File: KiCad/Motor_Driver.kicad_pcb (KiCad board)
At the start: 2 copper layers, 25 parts, among them J1 Battery Terminal, Q1 NMOS, Q2 NMOS, Q3 NMOS, Q4 NMOS, Q5 NMOS, Q6 NMOS, U1 PS2801-4

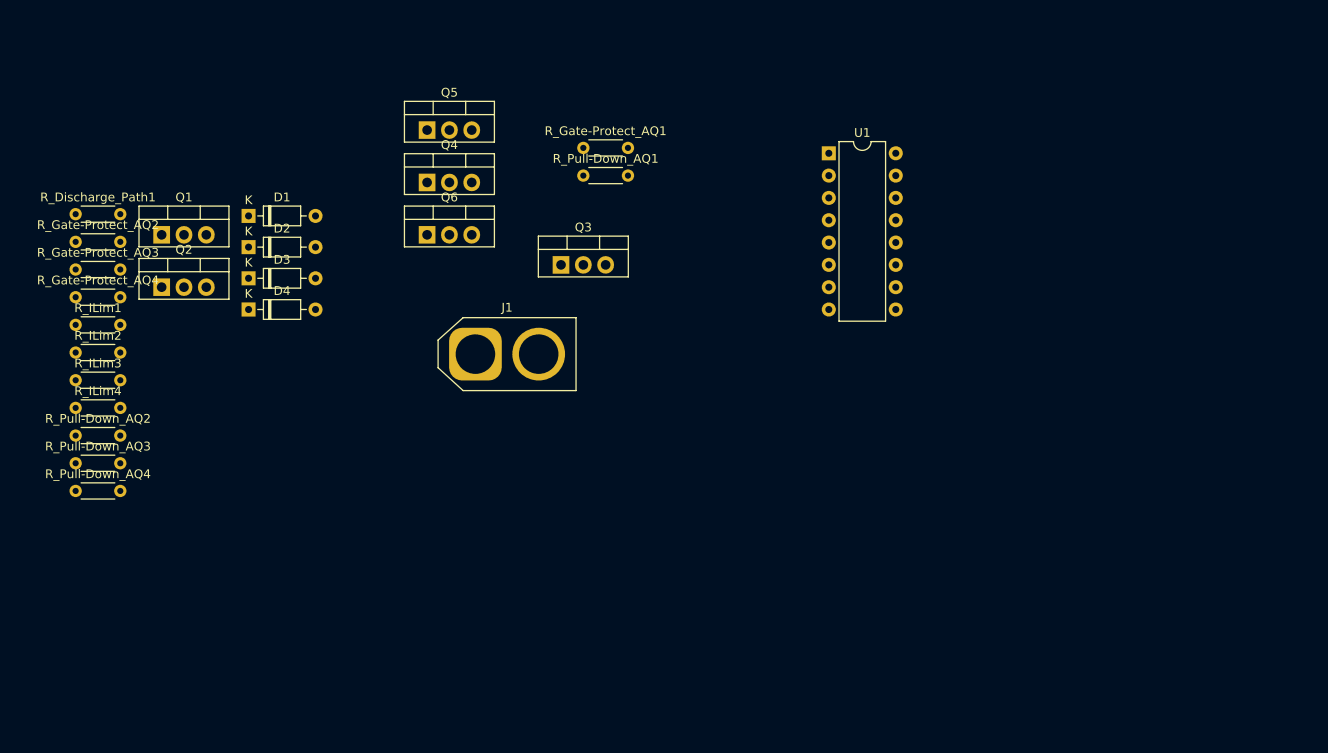
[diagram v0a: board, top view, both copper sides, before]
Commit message: Low Side Driver
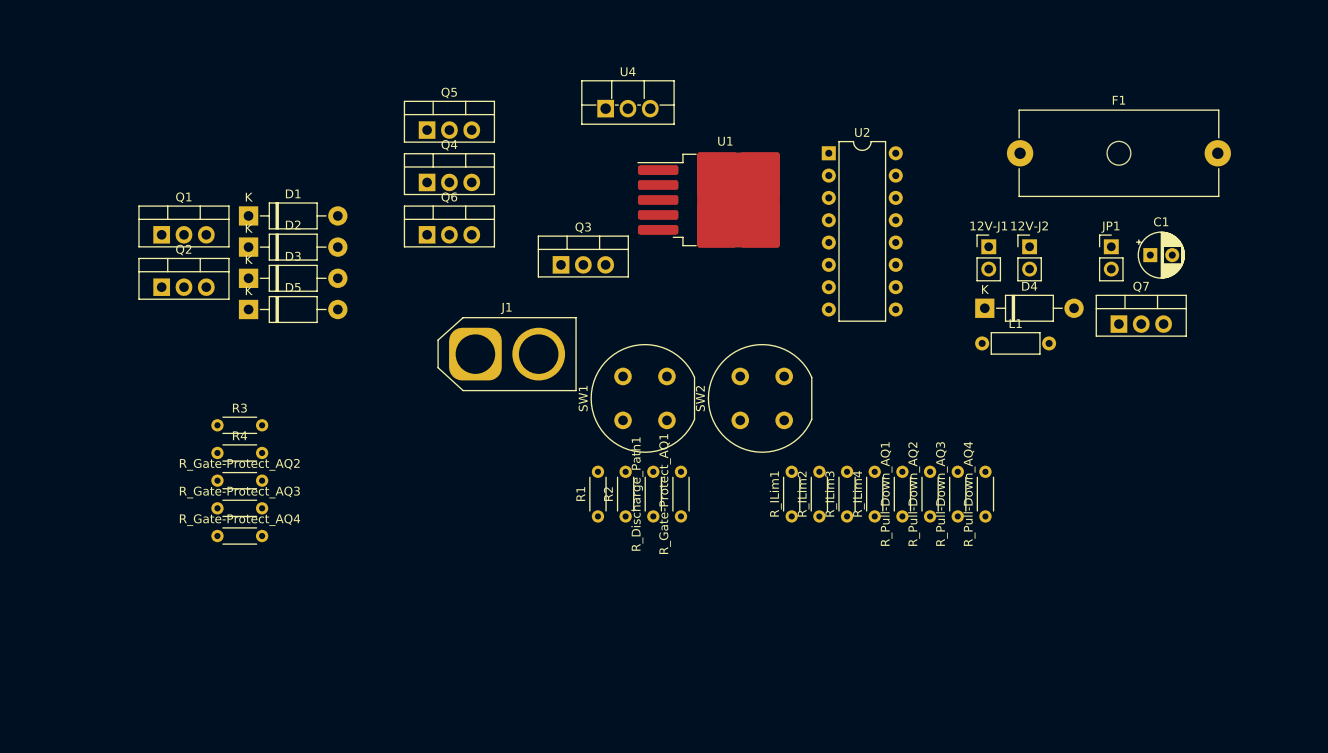
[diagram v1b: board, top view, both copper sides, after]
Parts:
- added 12V-J1: J-12V, Connector_PinHeader_2.54mm:PinHeader_1x02_P2.54mm_Vertical, F.Cu at (142.7, 51.3)
- added 12V-J2: J-12V, Connector_PinHeader_2.54mm:PinHeader_1x02_P2.54mm_Vertical, F.Cu at (147.3, 51.3)
- added C1: 10uF, Capacitor_THT:CP_Radial_D5.0mm_P2.50mm, F.Cu at (161.0, 52.2)
- added D4: 1N4007, Diode_THT:D_DO-41_SOD81_P10.16mm_Horizontal, F.Cu at (142.2, 58.3)
- added F1: Fuse_30A(Slow), Fuse:Fuseholder_Cylinder-5x20mm_Schurter_0031_8201_Horizontal_Open, F.Cu at (146.2, 40.6)
- added JP1: 24V-J1, Connector_PinHeader_2.54mm:PinHeader_1x02_P2.54mm_Vertical, F.Cu at (156.6, 51.3)
- added L1: 10mH, Inductor_THT:L_Axial_L5.3mm_D2.2mm_P7.62mm_Horizontal_Vishay_IM-1, F.Cu at (141.9, 62.3)
- added Q7: NMOS, Package_TO_SOT_THT:TO-220-3_Vertical, F.Cu at (157.5, 60.1)
- added R1: 500, Resistor_THT:R_Axial_DIN0204_L3.6mm_D1.6mm_P5.08mm_Horizontal, F.Cu at (98.2, 82.0)
- added R2: 10k, Resistor_THT:R_Axial_DIN0204_L3.6mm_D1.6mm_P5.08mm_Horizontal, F.Cu at (101.3, 82.0)
- added R3: 270, Resistor_THT:R_Axial_DIN0204_L3.6mm_D1.6mm_P5.08mm_Horizontal, F.Cu at (54.9, 71.6)
- added R4: 3.3k, Resistor_THT:R_Axial_DIN0204_L3.6mm_D1.6mm_P5.08mm_Horizontal, F.Cu at (54.9, 74.8)
- added SW1: DIR+A, Button_Switch_THT:Push_E-Switch_KS01Q01, F.Cu at (101.0, 71.0)
- added SW2: DIR-A, Button_Switch_THT:Push_E-Switch_KS01Q01, F.Cu at (114.4, 71.0)
- added U1: XL4015, Package_TO_SOT_SMD:TO-263-5_TabPin3, F.Cu at (112.7, 46.0)
- added U4: LM317T, Package_TO_SOT_THT:TO-220F-3_Vertical, F.Cu at (99.1, 35.6)
- D1, D2, D3: footprint Diode_THT:D_DO-35_SOD27_P7.62mm_Horizontal -> Diode_THT:D_DO-41_SOD81_P10.16mm_Horizontal
- D5: renamed from D4; footprint Diode_THT:D_DO-35_SOD27_P7.62mm_Horizontal -> Diode_THT:D_DO-41_SOD81_P10.16mm_Horizontal
- R_Gate-Protect_AQ1, R_Gate-Protect_AQ2, R_Gate-Protect_AQ3, R_Gate-Protect_AQ4: value 10 -> 100
- R_ILim1, R_ILim2, R_ILim3, R_ILim4: value 390 -> 250
- R_Pull-Down_AQ1, R_Pull-Down_AQ2, R_Pull-Down_AQ3, R_Pull-Down_AQ4: value 22k -> 100k
- moved R_Pull-Down_AQ4 103.6 mm to (142.3, 82.0), turned to 90 degrees
- moved R_Pull-Down_AQ3 100.6 mm to (139.1, 82.0), turned to 90 degrees
- moved R_Pull-Down_AQ2 97.7 mm to (136.0, 82.0), turned to 90 degrees
- moved R_ILim4 91.8 mm to (129.7, 82.0), turned to 90 degrees
- moved R_ILim3 89.2 mm to (126.5, 82.0), turned to 90 degrees
- moved R_ILim2 86.7 mm to (123.4, 82.0), turned to 90 degrees
- moved R_ILim1 84.4 mm to (120.2, 82.0), turned to 90 degrees
- moved R_Discharge_Path1 74.2 mm to (104.5, 82.0), turned to 90 degrees
- moved R_Pull-Down_AQ1 53.1 mm to (132.8, 82.0), turned to 90 degrees
- moved R_Gate-Protect_AQ1 43.4 mm to (107.6, 82.0), turned to 90 degrees
- moved R_Gate-Protect_AQ2 31.6 mm to (54.9, 77.9)
- moved R_Gate-Protect_AQ3 31.6 mm to (54.9, 81.0)
- moved R_Gate-Protect_AQ4 31.6 mm to (54.9, 84.2)
- renumbered U1 to U2
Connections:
- J1 pad 2: unconnected-(J1-Pin_2-Pad2) -> /V_Bat
- Q5 pad 3: /RPP_Source -> GND
- Q6 pad 3: /RPP_Source -> GND
- R_Discharge_Path1 pad 1: /MR-A -> /ML-A
- R_Discharge_Path1 pad 2: /ML-A -> /MR-A
- R_Gate-Protect_AQ1 pad 1: /GPow_Q1A -> /EmtrA1
- R_Gate-Protect_AQ1 pad 2: /EmtrA1 -> /GPow_Q1A
- R_Gate-Protect_AQ2 pad 1: /GPow_Q2A -> /EmtrA4
- R_Gate-Protect_AQ2 pad 2: /EmtrA2 -> /GPow_Q4A
- R_Gate-Protect_AQ3 pad 1: /GPow_Q3A -> /EmtrA3
- R_Gate-Protect_AQ3 pad 2: /EmtrA3 -> /GPow_Q3A
- R_Gate-Protect_AQ4 pad 1: /GPow_Q4A -> /EmtrA2
- R_Gate-Protect_AQ4 pad 2: /EmtrA4 -> /GPow_Q2A

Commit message: 5v5A supply
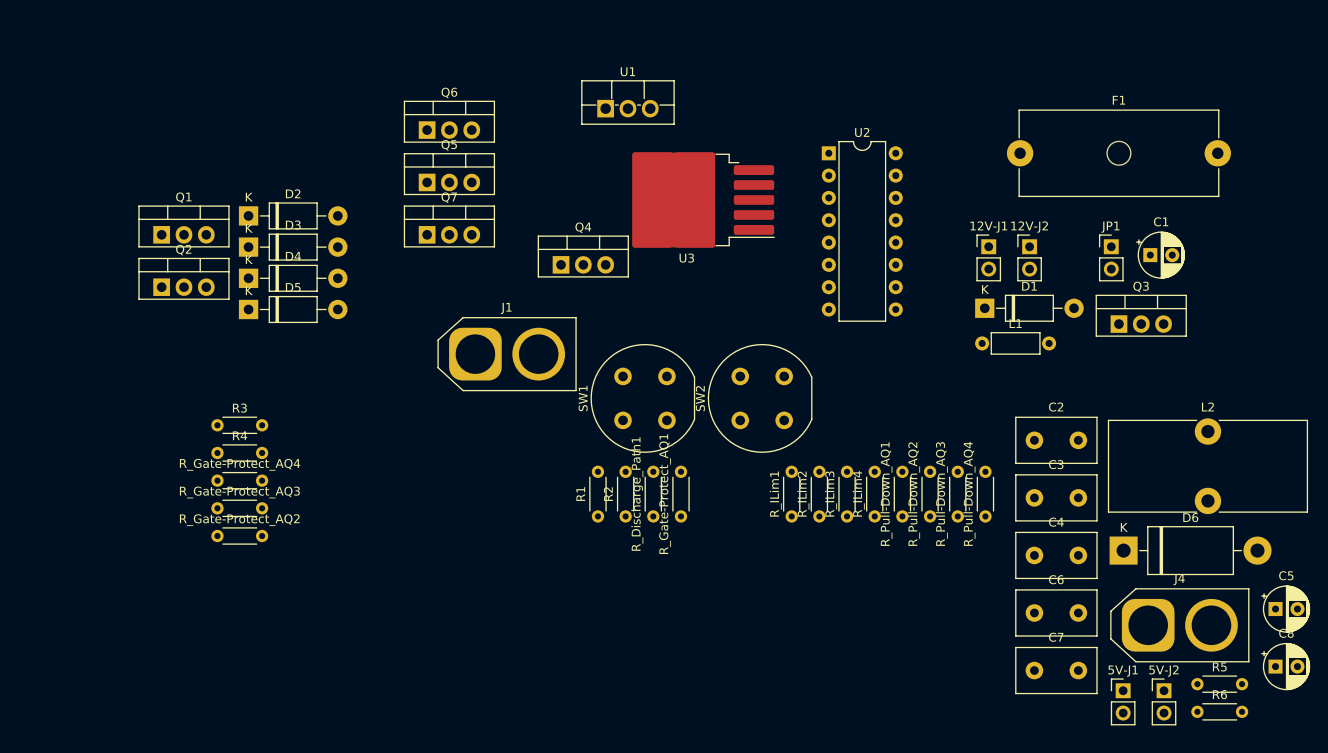
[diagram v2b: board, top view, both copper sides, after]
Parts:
- added 5V-J1: J-12V, Connector_PinHeader_2.54mm:PinHeader_1x02_P2.54mm_Vertical, F.Cu at (158.0, 101.8)
- added 5V-J2: J-12V, Connector_PinHeader_2.54mm:PinHeader_1x02_P2.54mm_Vertical, F.Cu at (162.6, 101.8)
- added C2: 100nF, Capacitor_THT:C_Disc_D9.0mm_W5.0mm_P5.00mm, F.Cu at (147.9, 73.3)
- added C3: 1uF, Capacitor_THT:C_Disc_D9.0mm_W5.0mm_P5.00mm, F.Cu at (147.9, 79.9)
- added C4: 1uF, Capacitor_THT:C_Disc_D9.0mm_W5.0mm_P5.00mm, F.Cu at (147.9, 86.4)
- added C5: 220uF, Capacitor_THT:CP_Radial_D5.0mm_P2.50mm, F.Cu at (175.3, 92.5)
- added C6: 1uF, Capacitor_THT:C_Disc_D9.0mm_W5.0mm_P5.00mm, F.Cu at (147.9, 93.0)
- added C7: 1uF, Capacitor_THT:C_Disc_D9.0mm_W5.0mm_P5.00mm, F.Cu at (147.9, 99.5)
- added C8: 330uF, Capacitor_THT:CP_Radial_D5.0mm_P2.50mm, F.Cu at (175.3, 99.1)
- added D6: 1N5822, Diode_THT:D_DO-201AD_P15.24mm_Horizontal, F.Cu at (158.0, 85.9)
- added J4: Motor_A, Connector_AMASS:AMASS_XT60-F_1x02_P7.20mm_Vertical, F.Cu at (160.8, 94.4)
- added L2: 47mH, Inductor_THT:L_Toroid_Vertical_L22.4mm_W10.2mm_P7.90mm_Vishay_TJ4, F.Cu at (167.6, 72.3)
- added R5: 10k, Resistor_THT:R_Axial_DIN0204_L3.6mm_D1.6mm_P5.08mm_Horizontal, F.Cu at (166.4, 101.1)
- added R6: 3.3k, Resistor_THT:R_Axial_DIN0204_L3.6mm_D1.6mm_P5.08mm_Horizontal, F.Cu at (166.4, 104.2)
- moved U3 4.39 mm to (108.3, 46.0), turned to 180 degrees
- renumbered D4 to D1, D1 to D2, D2 to D3, D3 to D4, Q7 to Q3, Q3 to Q4, Q4 to Q5, Q5 to Q6, Q6 to Q7, R_Gate-Protect_AQ4 to R_Gate-Protect_AQ2, R_Gate-Protect_AQ2 to R_Gate-Protect_AQ4, U4 to U1, U1 to U3
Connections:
- U3 pad 1: unconnected-(U1-GND-Pad1) -> GND2
- U3 pad 2: unconnected-(U1-FB-Pad2) -> Net-(U3-FB)
- U3 pad 3: unconnected-(U1-SW-Pad3) -> Net-(D6-K)
- U3 pad 4: unconnected-(U1-VC-Pad4) -> Net-(U3-VC)
- U3 pad 5: unconnected-(U1-VIN-Pad5) -> /Vcc

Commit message: Short Circuit Protection
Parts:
- removed R_Discharge_Path1: 100k, Resistor_THT:R_Axial_DIN0204_L3.6mm_D1.6mm_P5.08mm_Horizontal
- removed SW1: DIR+A, Button_Switch_THT:Push_E-Switch_KS01Q01
- removed SW2: DIR-A, Button_Switch_THT:Push_E-Switch_KS01Q01
- added D10: 1N4007, Diode_THT:D_DO-41_SOD81_P10.16mm_Horizontal, F.Cu at (107.1, 81.7)
- added D11: GREEN, LED_THT:LED_D3.0mm, F.Cu at (101.0, 89.2)
- added D12: 1N4007, Diode_THT:D_DO-41_SOD81_P10.16mm_Horizontal, F.Cu at (107.1, 85.9)
- added D7: BLUE, LED_THT:LED_D3.0mm_Clear, F.Cu at (101.0, 78.7)
- added D8: 1N4007, Diode_THT:D_DO-41_SOD81_P10.16mm_Horizontal, F.Cu at (107.1, 77.4)
- added D9: BLUE, LED_THT:LED_D3.0mm_Clear, F.Cu at (101.0, 83.6)
- added J3: MCU Terminals, Connector_JST:JST_EH_B7B-EH-A_1x07_P2.50mm_Vertical, F.Cu at (92.3, 72.1)
- added Q8: AO3405, Package_TO_SOT_SMD:SOT-23, F.Cu at (72.7, 87.0)
- added Q9: AO3400A, Package_TO_SOT_SMD:SOT-23, F.Cu at (79.7, 87.3)
- added R10: 10k, Resistor_THT:R_Axial_DIN0204_L3.6mm_D1.6mm_P5.08mm_Horizontal, F.Cu at (106.7, 99.1)
- added R7: 1.2k, Resistor_THT:R_Axial_DIN0204_L3.6mm_D1.6mm_P5.08mm_Horizontal, F.Cu at (106.7, 89.6)
- added R8: 1.2k, Resistor_THT:R_Axial_DIN0204_L3.6mm_D1.6mm_P5.08mm_Horizontal, F.Cu at (106.7, 92.8)
- added R9: 1.5k, Resistor_THT:R_Axial_DIN0204_L3.6mm_D1.6mm_P5.08mm_Horizontal, F.Cu at (106.7, 95.9)
- added SW3: DIR+A, Button_Switch_THT:SW_PUSH_6mm_H5mm, F.Cu at (90.8, 77.3)
- added SW4: DIR-A, Button_Switch_THT:SW_PUSH_6mm_H5mm, F.Cu at (90.8, 85.9)
- moved R1 38.4 mm to (134.6, 94.0)
- moved R2 30.7 mm to (129.5, 94.0)
- moved R_Gate-Protect_AQ1 20.7 mm to (124.5, 94.0)
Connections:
- R_ILim1 pad 1: /GSig_Q1A -> /LED_An_+_A
- R_ILim2 pad 1: /GSig_Q2A -> /LED_An_-_A
- R_ILim3 pad 1: /GSig_Q3A -> /LED_An_-_A
- R_ILim4 pad 1: /GSig_Q4A -> /LED_An_+_A
- U2 pad 2: GND2 -> /LED_Ct_+_A
- U2 pad 8: GND2 -> /LED_Ct_+_A

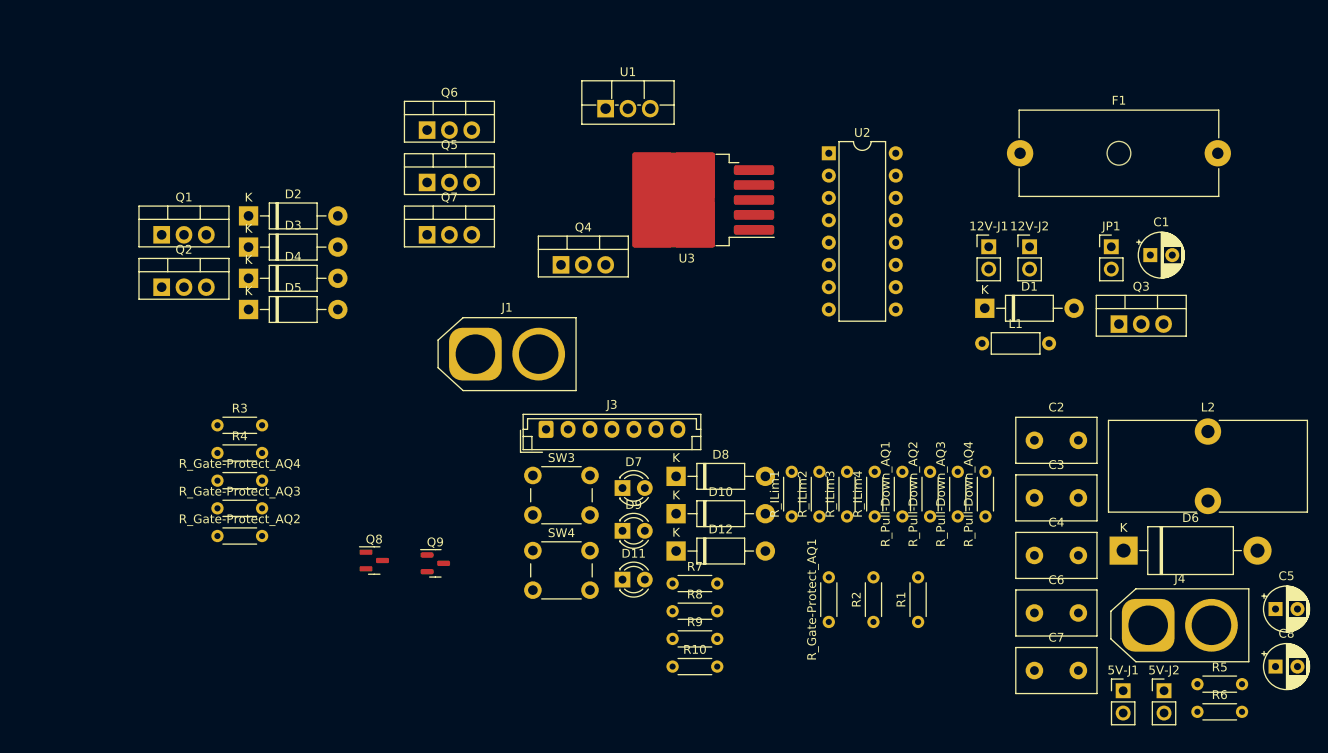
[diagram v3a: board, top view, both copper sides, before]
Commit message: Added NMOS Gate Drivers
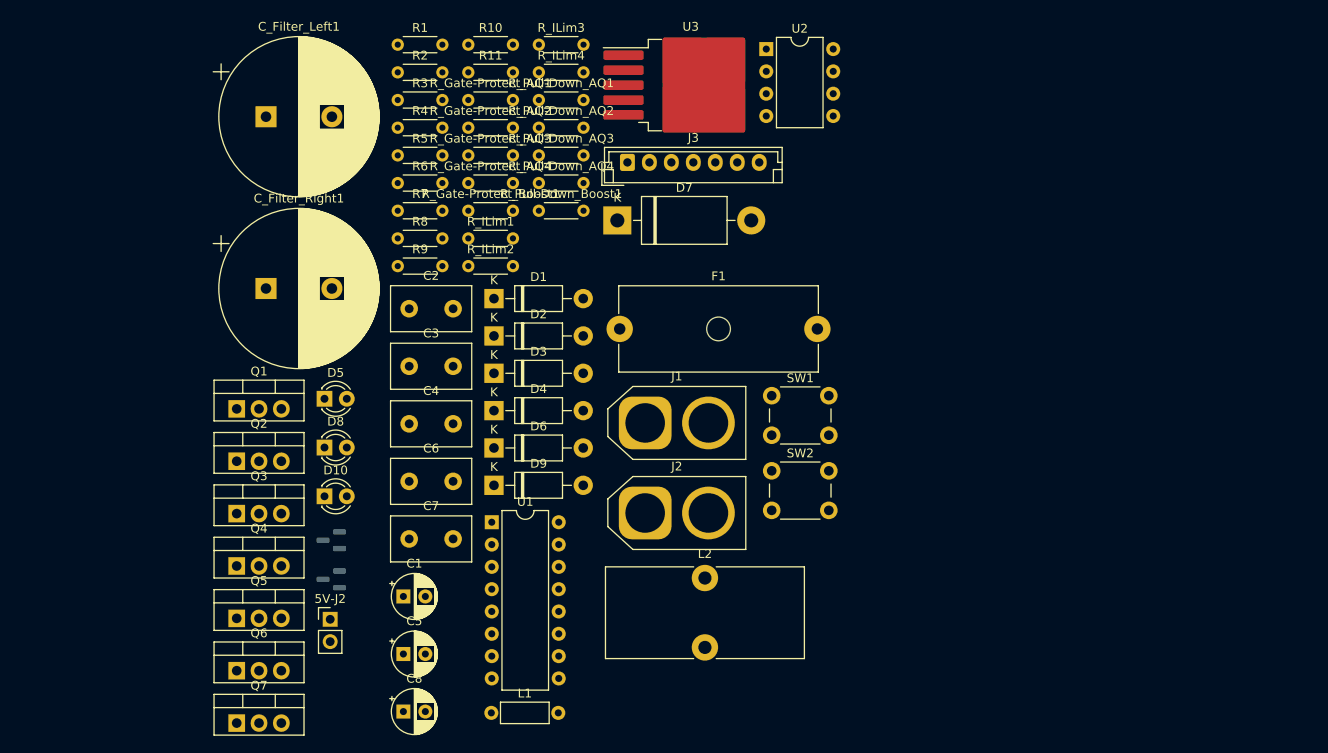
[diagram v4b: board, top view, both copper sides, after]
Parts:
- removed 12V-J1, 12V-J2, 5V-J1: J-12V, Connector_PinHeader_2.54mm:PinHeader_1x02_P2.54mm_Vertical
- removed D11: GREEN, LED_THT:LED_D3.0mm
- removed D12: 1N4007, Diode_THT:D_DO-41_SOD81_P10.16mm_Horizontal
- removed J4: Motor_A, Connector_AMASS:AMASS_XT60-F_1x02_P7.20mm_Vertical
- removed JP1: 24V-J1, Connector_PinHeader_2.54mm:PinHeader_1x02_P2.54mm_Vertical
- removed SW3: DIR+A, Button_Switch_THT:SW_PUSH_6mm_H5mm
- removed SW4: DIR-A, Button_Switch_THT:SW_PUSH_6mm_H5mm
- added C_Filter_Left1: 1000uF, Capacitor_THT:CP_Radial_D18.0mm_P7.50mm, F.Cu at (60.4, 36.5)
- added C_Filter_Right1: 1000uF, Capacitor_THT:CP_Radial_D18.0mm_P7.50mm, F.Cu at (60.4, 56.0)
- added J2: Motor_A, Connector_AMASS:AMASS_XT60-F_1x02_P7.20mm_Vertical, F.Cu at (103.6, 81.6)
- added R11: 1.5k, Resistor_THT:R_Axial_DIN0204_L3.6mm_D1.6mm_P5.08mm_Horizontal, F.Cu at (83.4, 31.4)
- added R_Gate-Protect_Boost1: 100, Resistor_THT:R_Axial_DIN0204_L3.6mm_D1.6mm_P5.08mm_Horizontal, F.Cu at (83.4, 47.2)
- added R_Pull-Down_Boost1: 100k, Resistor_THT:R_Axial_DIN0204_L3.6mm_D1.6mm_P5.08mm_Horizontal, F.Cu at (91.5, 47.2)
- added SW1: PWM_A, Button_Switch_THT:SW_PUSH_6mm_H5mm, F.Cu at (118.0, 68.2)
- added SW2: DIR_A, Button_Switch_THT:SW_PUSH_6mm_H5mm, F.Cu at (118.0, 76.8)
- C1: value 10uF -> 100uF
- C3: value 1uF -> 100nF
- D1: value 1N4007 -> 1N5352B
- D10: value 1N4007 -> GREEN; footprint Diode_THT:D_DO-41_SOD81_P10.16mm_Horizontal -> LED_THT:LED_D3.0mm
- D2, D4: value 1N5352B -> 1N4007
- D5: value 1N5352B -> BLUE; footprint Diode_THT:D_DO-41_SOD81_P10.16mm_Horizontal -> LED_THT:LED_D3.0mm_Clear
- D6: value 1N5822 -> 1N4007; footprint Diode_THT:D_DO-201AD_P15.24mm_Horizontal -> Diode_THT:D_DO-41_SOD81_P10.16mm_Horizontal
- D7: value BLUE -> 1N5822; footprint LED_THT:LED_D3.0mm_Clear -> Diode_THT:D_DO-201AD_P15.24mm_Horizontal
- D8: value 1N4007 -> BLUE; footprint Diode_THT:D_DO-41_SOD81_P10.16mm_Horizontal -> LED_THT:LED_D3.0mm_Clear
- D9: value BLUE -> 1N4007; footprint LED_THT:LED_D3.0mm_Clear -> Diode_THT:D_DO-41_SOD81_P10.16mm_Horizontal
- Q8, Q9: moved to B.Cu
- R1: value 500 -> 100
- R10: value 10k -> 1.2k
- R2: value 10k -> 68k
- R3: value 270 -> 33k
- R4: value 3.3k -> 1k
- R5: value 10k -> 33k
- R6: value 3.3k -> 10k
- R8: value 1.2k -> 10k
- R9: value 1.5k -> 3.3k
- U1: value LM317T -> PS2801-4; footprint Package_TO_SOT_THT:TO-220F-3_Vertical -> Package_DIP:DIP-16_W7.62mm
- U2: value PS2801-4 -> NE555P; footprint Package_DIP:DIP-16_W7.62mm -> Package_DIP:DIP-8_W7.62mm
- moved R5 109.1 mm to (75.4, 40.9)
- moved R6 109.1 mm to (75.4, 44.0)
- moved Q3 102.7 mm to (57.1, 81.7)
- moved C5 99.4 mm to (76.0, 97.6)
- moved C8 99.4 mm to (76.0, 104.2)
- moved 5V-J2 95.2 mm to (67.7, 93.7)
- moved C1 93.5 mm to (76.0, 91.1)
- moved R1 88.5 mm to (75.4, 28.3), turned to 0 degrees
- moved R2 82.7 mm to (75.4, 31.4), turned to 0 degrees
- moved R10 74.5 mm to (83.4, 28.3)
- moved C2 72.7 mm to (76.7, 58.3)
- moved C3 72.7 mm to (76.7, 64.9)
- moved C4 72.7 mm to (76.7, 71.4)
- moved C6 72.7 mm to (76.7, 78.0)
- moved C7 72.7 mm to (76.7, 84.5)
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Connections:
- C2 pad 1: Net-(12V-J2-B) -> Net-(U2-THRES)
- C3 pad 1: /V_LS-A -> Net-(U2-CONT)
- C7 pad 1: Net-(5V-J1-A) -> /+5V
- C8 pad 1: Net-(5V-J1-A) -> /+5V
- D1 pad 1: /V_HS-A -> /Vcc
- D1 pad 2: Net-(D1-A) -> /V_HS-A
- D10 pad 1: /ML-A -> Net-(D10-K)
- D10 pad 2: Net-(D10-A) -> /Vcc
- D2 pad 1: /GPow_Q1A -> /V_HS-A
- D2 pad 2: /ML-A -> Net-(D2-A)
- D3 pad 1: /GPow_Q2A -> /V_LS-A
- D3 pad 2: /MR-A -> GND
- D4 pad 1: /GPow_Q3A -> /DIR_A
- D4 pad 2: GND -> Net-(D4-A)
- D5 pad 1: /GPow_Q4A -> Net-(D5-K)
- D5 pad 2: GND -> /ML-A
- D6 pad 1: Net-(D6-K) -> /MR-A
- D6 pad 2: GND2 -> Net-(D6-A)
- D7 pad 2: /ML-A -> GND2
- D8 pad 1: /MR-A -> Net-(D8-K)
- D8 pad 2: Net-(D8-A) -> /MR-A
- D9 pad 1: Net-(D9-K) -> /ML-A
- D9 pad 2: /MR-A -> Net-(D9-A)
- L1 pad 2: Net-(D1-A) -> Net-(D2-A)
- L2 pad 1: Net-(D6-K) -> Net-(D7-K)
- L2 pad 2: Net-(5V-J1-A) -> /+5V
- Q3 pad 1: /V_Gate-Boost -> /GPow_Q1A
- Q3 pad 2: Net-(D1-A) -> Net-(Q1-D)
- Q3 pad 3: GND -> /ML-A
- Q4 pad 1: /GPow_Q1A -> /GPow_Q2A
- Q4 pad 2: Net-(Q1-D) -> Net-(Q2-D)
- Q4 pad 3: /ML-A -> /MR-A
- Q5 pad 1: /GPow_Q2A -> /GPow_Q3A
- Q5 pad 2: Net-(Q2-D) -> /ML-A
- Q5 pad 3: /MR-A -> GND
- Q6 pad 1: /GPow_Q3A -> /GPow_Q4A
- Q6 pad 2: /ML-A -> /MR-A
- Q7 pad 1: /GPow_Q4A -> /V_Gate-Boost
- Q7 pad 2: /MR-A -> Net-(D2-A)
- Q8 pad 1: Net-(D12-A) -> Net-(D4-A)
- R10 pad 1: GND2 -> Net-(D9-A)
- R10 pad 2: /DIR_A -> Net-(D8-K)
- R3 pad 1: Net-(U1-ADJ) -> /V_HS-A
- R4 pad 1: GND -> Net-(U2-DISCH)
- R4 pad 2: Net-(U1-ADJ) -> /V_LS-A
- R5 pad 1: Net-(U3-FB) -> Net-(U2-THRES)
- R5 pad 2: Net-(5V-J1-A) -> Net-(U2-DISCH)
- R6 pad 2: Net-(U3-FB) -> /DIR_A
- R7 pad 1: Net-(D8-A) -> Net-(D6-A)
- R7 pad 2: Net-(D7-K) -> Net-(D5-K)
- R8 pad 1: Net-(D10-A) -> Net-(U3-FB)
- R8 pad 2: Net-(D9-K) -> /+5V
- R9 pad 1: GND -> GND2
- R9 pad 2: Net-(D11-K) -> Net-(U3-FB)
- R_ILim1 pad 2: Net-(U2-A1) -> Net-(U1-A1)
- R_ILim2 pad 2: Net-(U2-A2) -> Net-(U1-A2)
- R_ILim3 pad 2: Net-(U2-A3) -> Net-(U1-A3)
- R_ILim4 pad 2: Net-(U2-A4) -> Net-(U1-A4)
- U1 pad 1: Net-(U1-ADJ) -> Net-(U1-A1)
- U1 pad 2: /V_LS-A -> /LED_Ct_+_A
- U1 pad 3: Net-(12V-J2-B) -> Net-(U1-A2)
- U2 pad 1: Net-(U2-A1) -> GND
- U2 pad 2: /LED_Ct_+_A -> Net-(U2-THRES)
- U2 pad 3: Net-(U2-A2) -> Net-(U2-OUT)
- U2 pad 4: GND2 -> /V_LS-A
- U2 pad 5: Net-(U2-A3) -> Net-(U2-CONT)
- U2 pad 6: GND2 -> Net-(U2-THRES)
- U2 pad 7: Net-(U2-A4) -> Net-(U2-DISCH)
- U2 pad 8: /LED_Ct_+_A -> /V_LS-A
- U3 pad 3: Net-(D6-K) -> Net-(D7-K)
